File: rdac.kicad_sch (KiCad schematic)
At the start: 18 parts

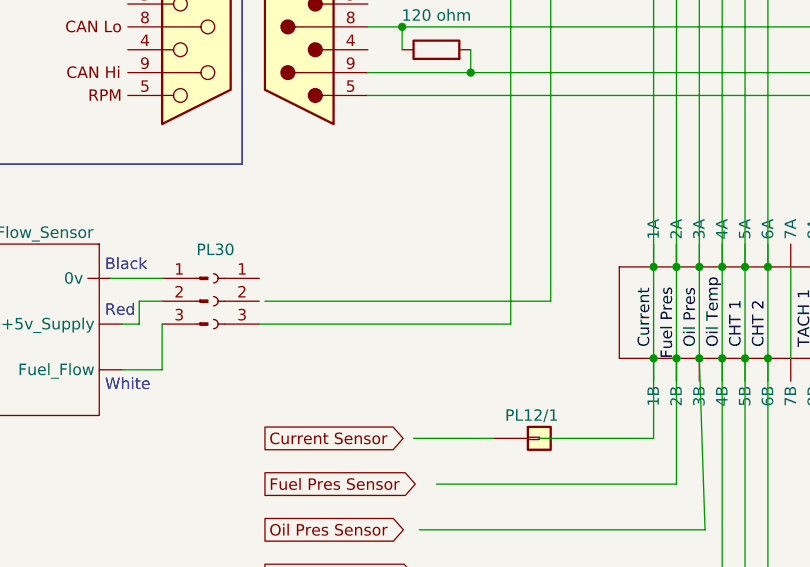
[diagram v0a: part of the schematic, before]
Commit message: Added fuel flow sensor ground connection
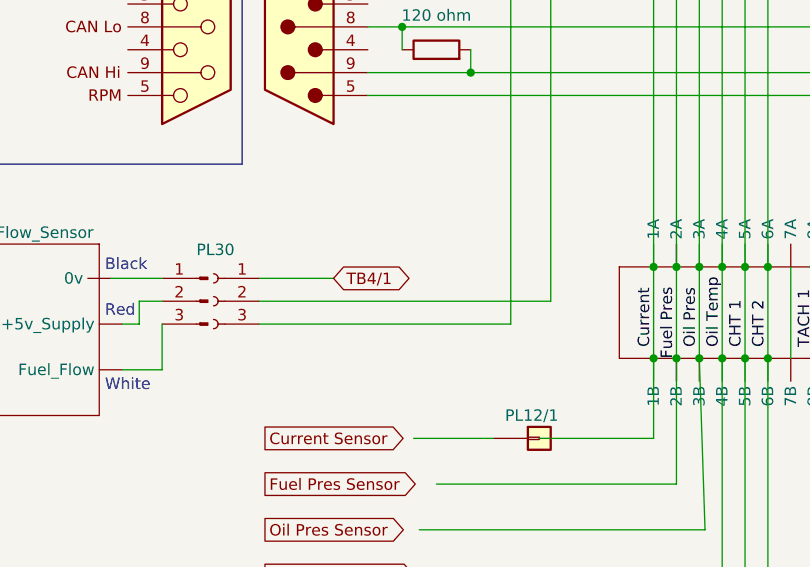
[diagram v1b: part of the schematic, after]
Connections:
- net at FB2/2.1: now also J?.2 (Pin_2)
- net TB4/1: now reaches J?.1 (Pin_1)
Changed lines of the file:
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@@
   (title_block
     (title "Europa RDAC wiring")
-    (date "2022-12-30")
-    (rev "3")
+    (date "2023-01-03")
+    (rev "4")
   )
   (junction (at 127 147.32) (diameter 0) (color 0 0 0 0)
@@
     (stroke (width 0) (type default) (color 0 0 0 0))
   )
-  (wire (pts (xy 66.04 151.13) (xy 97.79 151.13))
+  (wire (pts (xy 65.405 151.13) (xy 97.79 151.13))
     (stroke (width 0) (type default) (color 0 0 0 0))
   )
@@
   )
   (wire (pts (xy 178.435 86.36) (xy 180.34 86.36))
+    (stroke (width 0) (type default) (color 0 0 0 0))
+  )
+  (wire (pts (xy 65.405 148.59) (xy 73.66 148.59))
     (stroke (width 0) (type default) (color 0 0 0 0))
   )
@@
       (effects (font (size 1.27 1.27)) (justify left) hide)
     )
+  )
+  (global_label "TB4{slash}1" (shape bidirectional) (at 73.66 148.59 0) (fields_autoplaced)
+    (effects (font (size 1.27 1.27)) (justify left))
+    (property "Intersheet References" "${INTERSHEET_REFS}" (id 0) (at 82.0602 148.5106 0)
+      (effects (font (size 1.27 1.27)) (justify left) hide)
+    )
